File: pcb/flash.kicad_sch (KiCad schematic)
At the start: 7 parts, among them U8 GD5F2GM7UEYIGR

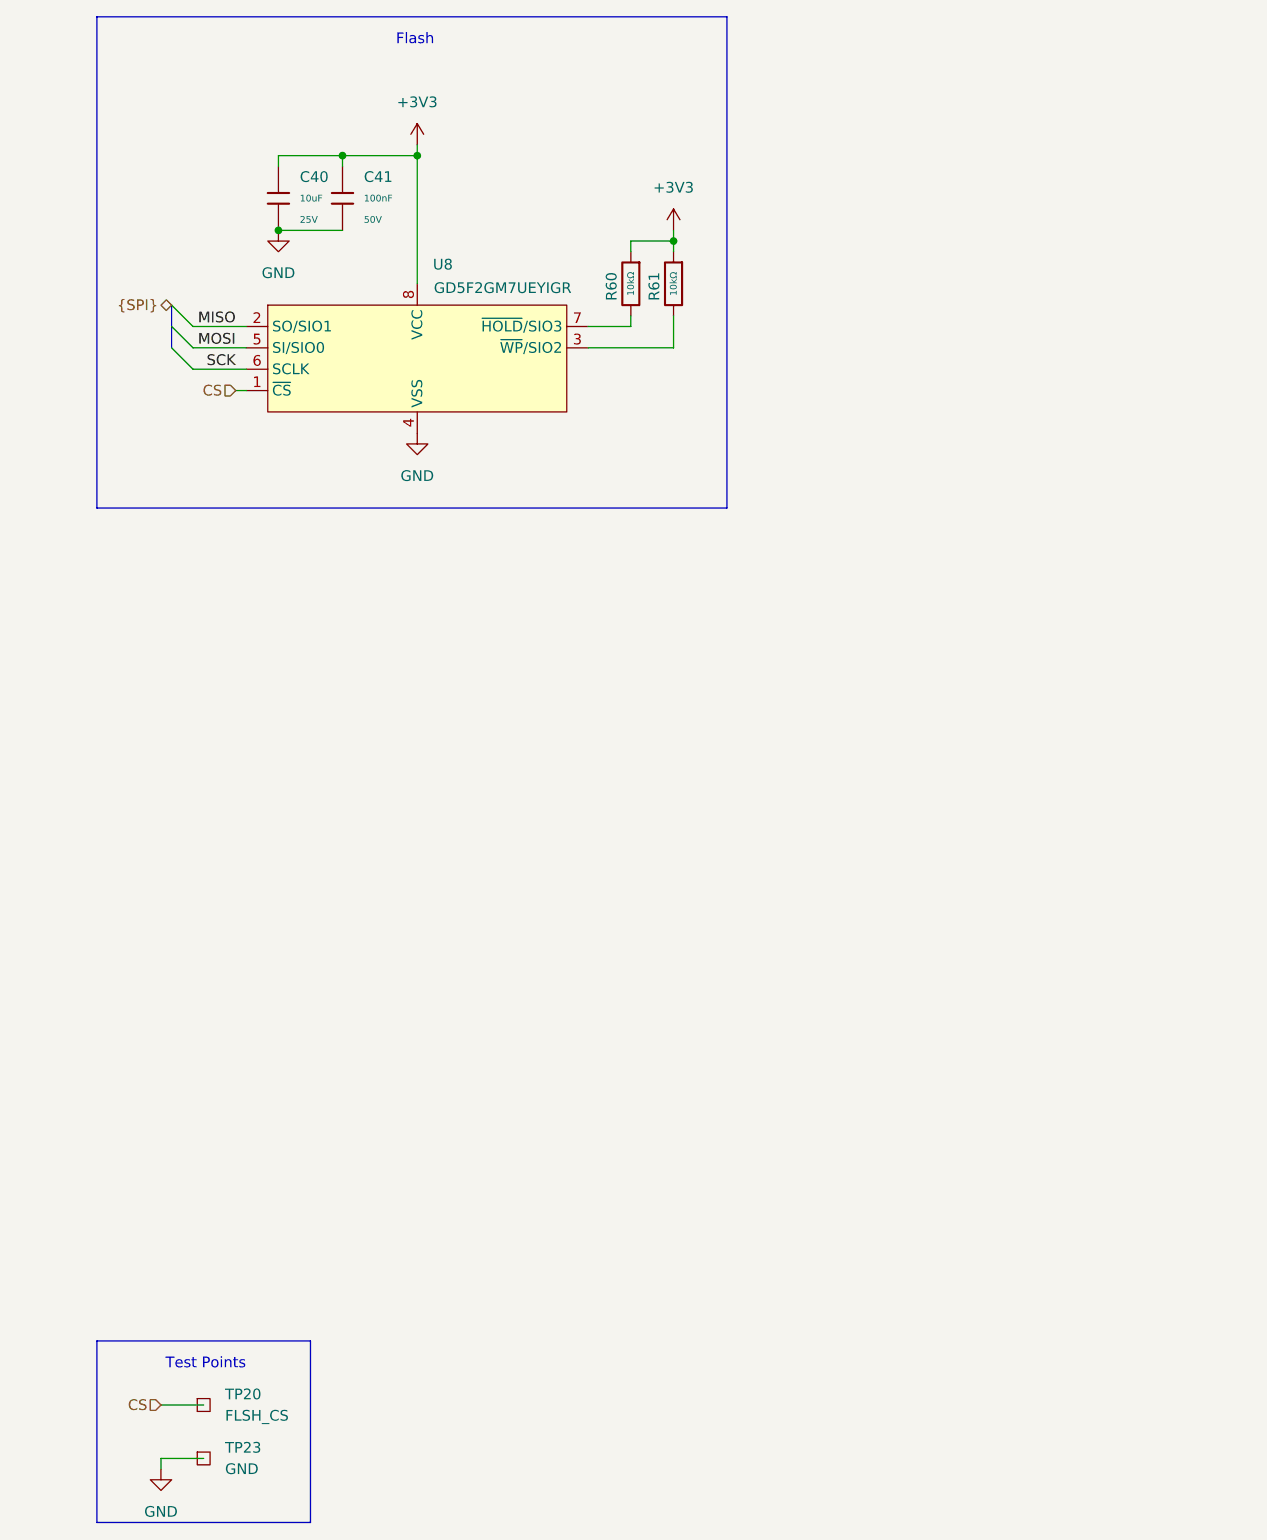
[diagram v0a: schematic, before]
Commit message: sch: rewire SPI to supply separate clock lines to flash and ethernet
The flash IC datasheet specifies that the SPI clock must not be toggled
while CS is high, which means we need to separate the ethernet and flash
clock lines.

I've GPIO3 on the ESP for the flash clock line, and plan to use the
internal peripheral MUX to switch it when talking with the IC.

I've also moved a bunch of test points and termination resistors in this
process.
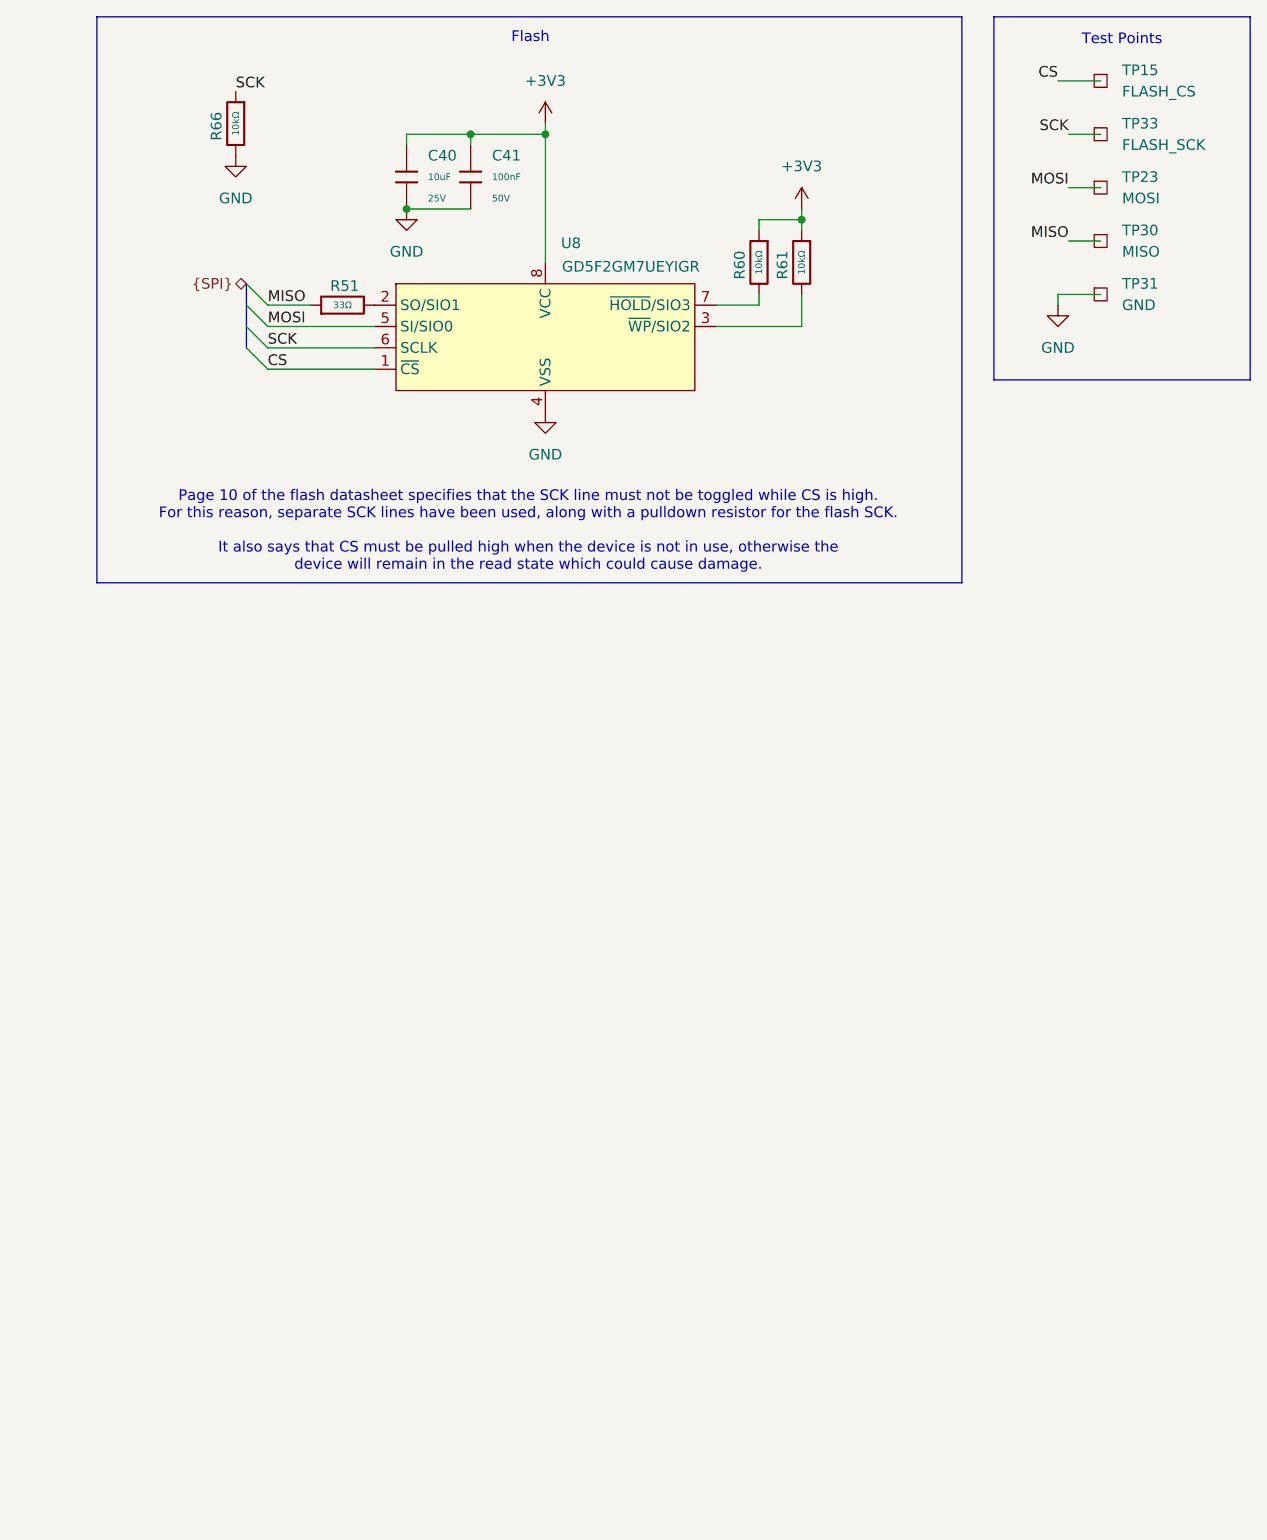
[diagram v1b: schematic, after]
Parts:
- removed TP20: FLSH_CS, TestPoint:TestPoint_Pad_D1.0mm, symbol Connector:TestPoint_Square
- added R51: 33Ω, PCM_JLCPCB:R_0603, symbol PCM_JLCPCB-Resistors:0603,33Ω
- added R66: 10kΩ, PCM_JLCPCB:R_0603, symbol PCM_JLCPCB-Resistors:0603,10kΩ
- added TP15: FLASH_CS, TestPoint:TestPoint_Pad_D1.0mm, symbol Connector:TestPoint_Square
- added TP30: MISO, TestPoint:TestPoint_Pad_D1.0mm, symbol Connector:TestPoint_Square
- added TP31: GND, TestPoint:TestPoint_Plated_Hole_D2.0mm, symbol Connector:TestPoint_Square
- added TP33: FLASH_SCK, TestPoint:TestPoint_Pad_D1.0mm, symbol Connector:TestPoint_Square
- TP23: value GND -> MOSI; footprint TestPoint:TestPoint_Plated_Hole_D2.0mm -> TestPoint:TestPoint_Pad_D1.0mm; now left out of the parts list
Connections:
- net CS: now also TP15.1
- net GND: now also R66.2, TP31.1; no longer TP23.1
- net MISO: now also R51.1, TP30.1; no longer U8.2 (SO/SIO1)
- net MOSI: now also TP23.1
- net SCK: now also R66.1, TP33.1
- new net: R51.2, U8.2 (SO/SIO1)
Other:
- note added: "Page 10 of the flash datasheet specifies that the SCK line must not be toggled while CS is high. For this reason, separate SCK lines have been used, along with a pulldown resistor for the flash SCK. It also says that CS must be pulled high when the device is not in use, otherwise the device will remain in the read state which could cause damage."
- moved on the sheet: C40, C41, R60, R61, U8

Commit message: pcb: route remaining tracks
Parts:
- removed TP30: MISO, TestPoint:TestPoint_Pad_D1.0mm, symbol Connector:TestPoint_Square
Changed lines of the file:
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@@
-	(wire
-		(pts
-			(xy 130.81 41.91) (xy 134.62 41.91)
-		)
-		(stroke
-			(width 0)
-			(type default)
-		)
-	)
 	(wire
 		(pts
@@
 	(label "MOSI"
 		(at 130.81 35.56 180)
-		(effects
-			(font
-				(size 1.27 1.27)
-			)
-			(justify right bottom)
-		)
-	)
-	(label "MISO"
-		(at 130.81 41.91 180)
 		(effects
 			(font
@@
 					(unit 1)
 				)
-			)
-		)
-	)
-	(symbol
-		(lib_id "Connector:TestPoint_Square")
-		(at 134.62 41.91 0)
-		(unit 1)
-		(body_style 1)
-		(exclude_from_sim no)
-		(in_bom no)
-		(on_board yes)
-		(in_pos_files no)
-		(dnp no)
-		(fields_autoplaced yes)
-		(property "Reference" "TP30"
-			(at 137.16 40.6399 0)
-			(show_name no)
-			(do_not_autoplace no)
-			(effects
-				(font
-					(size 1.27 1.27)
-				)
-				(justify left)
-			)
-		)
-		(property "Value" "MISO"
-			(at 137.16 43.1799 0)
-			(show_name no)
-			(do_not_autoplace no)
-			(effects
-				(font
-					(size 1.27 1.27)
-				)
-				(justify left)
-			)
-		)
-		(property "Footprint" "TestPoint:TestPoint_Pad_D1.0mm"
-			(at 139.7 41.91 0)
-			(hide yes)
-			(show_name no)
-			(do_not_autoplace no)
-			(effects
-				(font
-					(size 1.27 1.27)
-				)
-			)
-		)
-		(property "Datasheet" "~"
-			(at 139.7 41.91 0)
-			(hide yes)
-			(show_name no)
-			(do_not_autoplace no)
-			(effects
-				(font
-					(size 1.27 1.27)
-				)
-			)
-		)
-		(property "Description" "test point"
-			(at 134.62 41.91 0)
-			(hide yes)
-			(show_name no)
-			(do_not_autoplace no)
-			(effects
-				(font
-					(size 1.27 1.27)
-				)
-			)
-		)
-		(property "Average Rectified Current (Io)" ""
-			(at 134.62 41.91 0)
-			(hide yes)
-			(show_name no)
-			(do_not_autoplace no)
-			(effects
-				(font
-					(size 1.27 1.27)
-				)
-			)
-		)
-		(property "Clamping Voltage" ""
-			(at 134.62 41.91 0)
-			(hide yes)
-			(show_name no)
-			(do_not_autoplace no)
-			(effects
-				(font
-					(size 1.27 1.27)
-				)
-			)
-		)
-		(property "LSCS Part" ""
-			(at 134.62 41.91 0)
-			(hide yes)
-			(show_name no)
-			(do_not_autoplace no)
-			(effects
-				(font
-					(size 1.27 1.27)
-				)
-			)
-		)
-		(property "Number of Channels" ""
-			(at 134.62 41.91 0)
-			(hide yes)
-			(show_name no)
-			(do_not_autoplace no)
-			(effects
-				(font
-					(size 1.27 1.27)
-				)
-			)
-		)
-		(property "Peak Pulse Current (Ipp)" ""
-			(at 134.62 41.91 0)
-			(hide yes)
-			(show_name no)
-			(do_not_autoplace no)
-			(effects
-				(font
-					(size 1.27 1.27)
-				)
-			)
-		)
-		(property "Peak Pulse Power Dissipation (Ppp)" ""
-			(at 134.62 41.91 0)
-			(hide yes)
-			(show_name no)
-			(do_not_autoplace no)
-			(effects
-				(font
-					(size 1.27 1.27)
-				)
-			)
-		)
-		(property "Peak forward surge current" ""
-			(at 134.62 41.91 0)
-			(hide yes)
-			(show_name no)
-			(do_not_autoplace no)
-			(effects
-				(font
-					(size 1.27 1.27)
-				)
-			)
-		)
-		(property "Polarity" ""
-			(at 134.62 41.91 0)
-			(hide yes)
-			(show_name no)
-			(do_not_autoplace no)
-			(effects
-				(font
-					(size 1.27 1.27)
-				)
-			)
-		)
-		(property "Voltage - Breakdown" ""
-			(at 134.62 41.91 0)
-			(hide yes)
-			(show_name no)
-			(do_not_autoplace no)
-			(effects
-				(font
-					(size 1.27 1.27)
-				)
-			)
-		)
-		(property "level of protection" ""
-			(at 134.62 41.91 0)
-			(hide yes)
-			(show_name no)
-			(do_not_autoplace no)
-			(effects
-				(font
-					(size 1.27 1.27)
-				)
-			)
-		)
-		(pin "1"
-		)
-		(instances
-			(project "EveningStar"
-				(path "/4c61f5a2-f8d4-462a-9bc3-d74437d30372/461540ed-57ef-4b9a-99b0-62364a0e276f"
-					(reference "TP30")
-					(unit 1)
-				)

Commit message: pcb: fix most drc errors
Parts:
- TP15, TP23, TP33: footprint TestPoint:TestPoint_Pad_D1.0mm -> custom:TestPoint_Pad_D1.0mm
- TP31: footprint TestPoint:TestPoint_Plated_Hole_D2.0mm -> custom:TestPoint_Plated_Hole_D2.0mm
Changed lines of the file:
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@@
 			)
 		)
-		(property "Footprint" "TestPoint:TestPoint_Pad_D1.0mm"
+		(property "Footprint" "custom:TestPoint_Pad_D1.0mm"
 			(at 139.7 29.21 0)
 			(hide yes)
@@
 			)
 		)
-		(property "Footprint" "TestPoint:TestPoint_Pad_D1.0mm"
+		(property "Footprint" "custom:TestPoint_Pad_D1.0mm"
 			(at 139.7 22.86 0)
 			(hide yes)
@@
 			)
 		)
-		(property "Footprint" "TestPoint:TestPoint_Pad_D1.0mm"
+		(property "Footprint" "custom:TestPoint_Pad_D1.0mm"
 			(at 139.7 35.56 0)
 			(hide yes)
@@
 			)
 		)
-		(property "Footprint" "TestPoint:TestPoint_Plated_Hole_D2.0mm"
+		(property "Footprint" "custom:TestPoint_Plated_Hole_D2.0mm"
 			(at 139.7 48.26 0)
 			(hide yes)
